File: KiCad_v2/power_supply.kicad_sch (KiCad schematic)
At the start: 45 parts, among them U1 TPS55340RTER, U6 MCP73871, U8 TPS54331

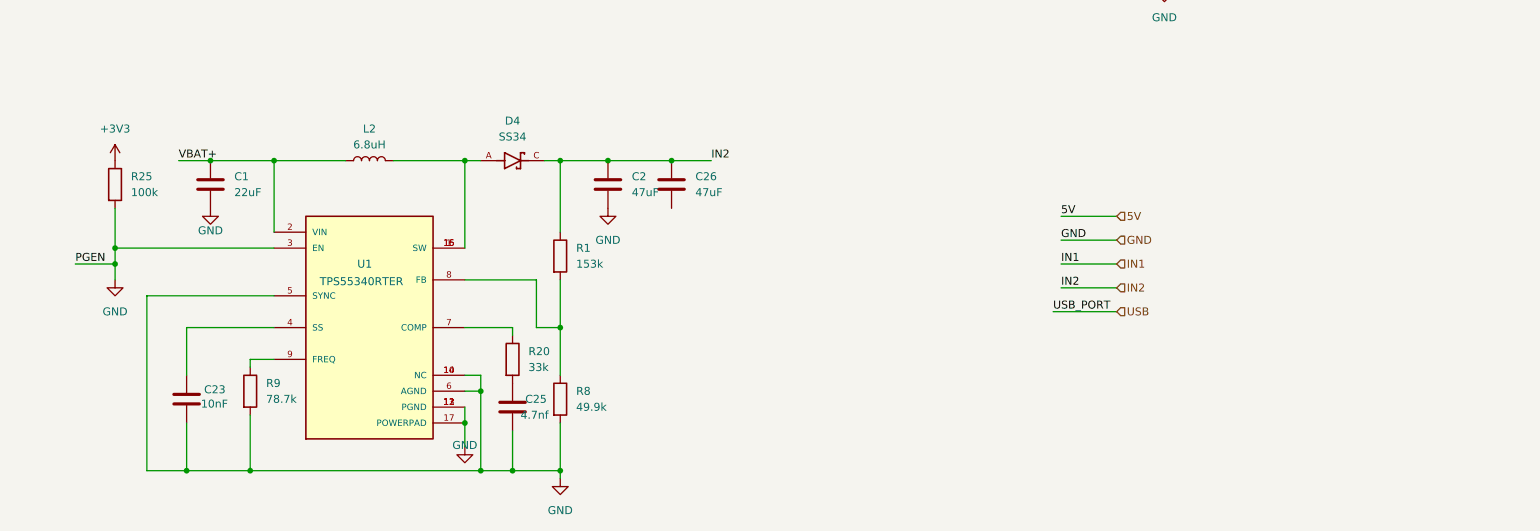
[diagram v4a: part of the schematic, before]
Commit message: agrego LT8582
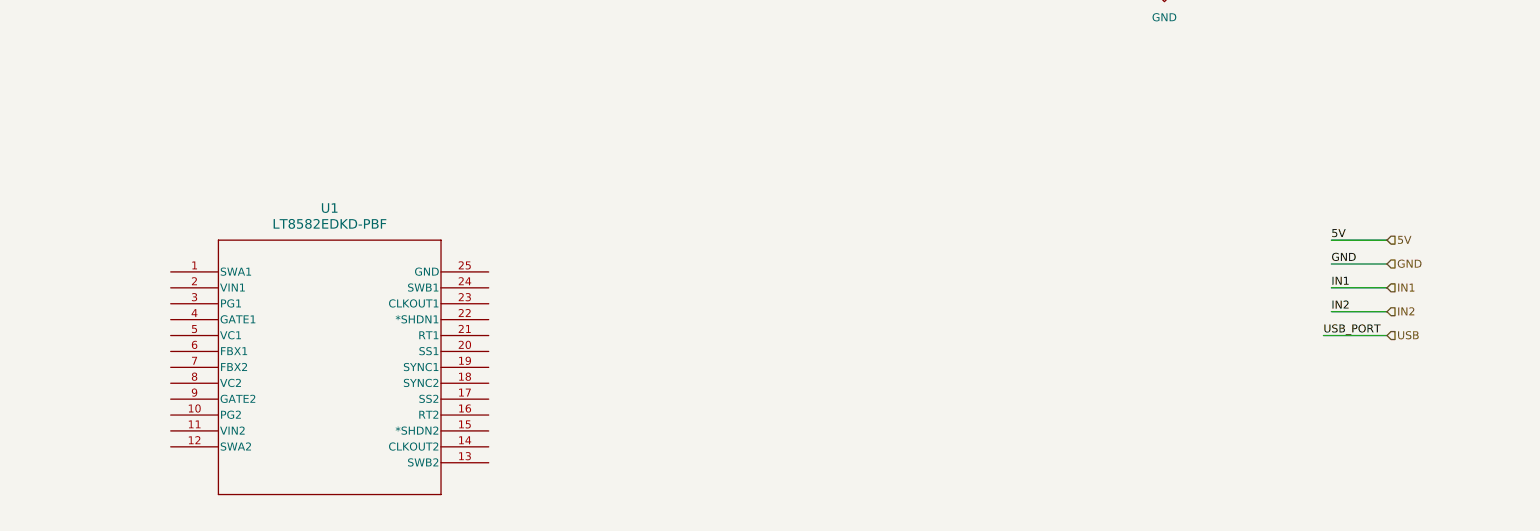
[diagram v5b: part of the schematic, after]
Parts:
- removed C1: 22uF, Capacitor_SMD:C_0603_1608Metric, symbol Device:C
- removed C2, C26: 47uF, Capacitor_SMD:C_0603_1608Metric, symbol Device:C
- removed C23: 10nF, Capacitor_SMD:C_0603_1608Metric, symbol Device:C
- removed C25: 4.7nf, Capacitor_SMD:C_0603_1608Metric, symbol Device:C
- removed D4: SS34, Custom_Footprints:DIOM7959X265N, symbol SS34:SS34
- removed L2: 6.8uH, Custom_Footprints:IND_SRP6540-100M, symbol Device:L
- removed R1: 153k, Resistor_SMD:R_0603_1608Metric, symbol Device:R
- removed R20: 33k, Resistor_SMD:R_0603_1608Metric, symbol Device:R
- removed R25: 100k, Resistor_SMD:R_0603_1608Metric, symbol Device:R
- removed R8: 49.9k, Resistor_SMD:R_0603_1608Metric, symbol Device:R
- removed R9: 78.7k, Resistor_SMD:R_0603_1608Metric, symbol Device:R
- removed U1: TPS55340RTER, Custom_Footprints:QFN50P300X300X80-17N, symbol TPS55340RTER:TPS55340RTER
- added U1: LT8582EDKD-PBF, Custom_Footprints:DKD_ADI-M, symbol LT8582:LT8582EDKD-PBF
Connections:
- net GND: no longer R6.1, U6.6 (~{PG})
- new net PGEN: R6.1, U6.6 (~{PG})

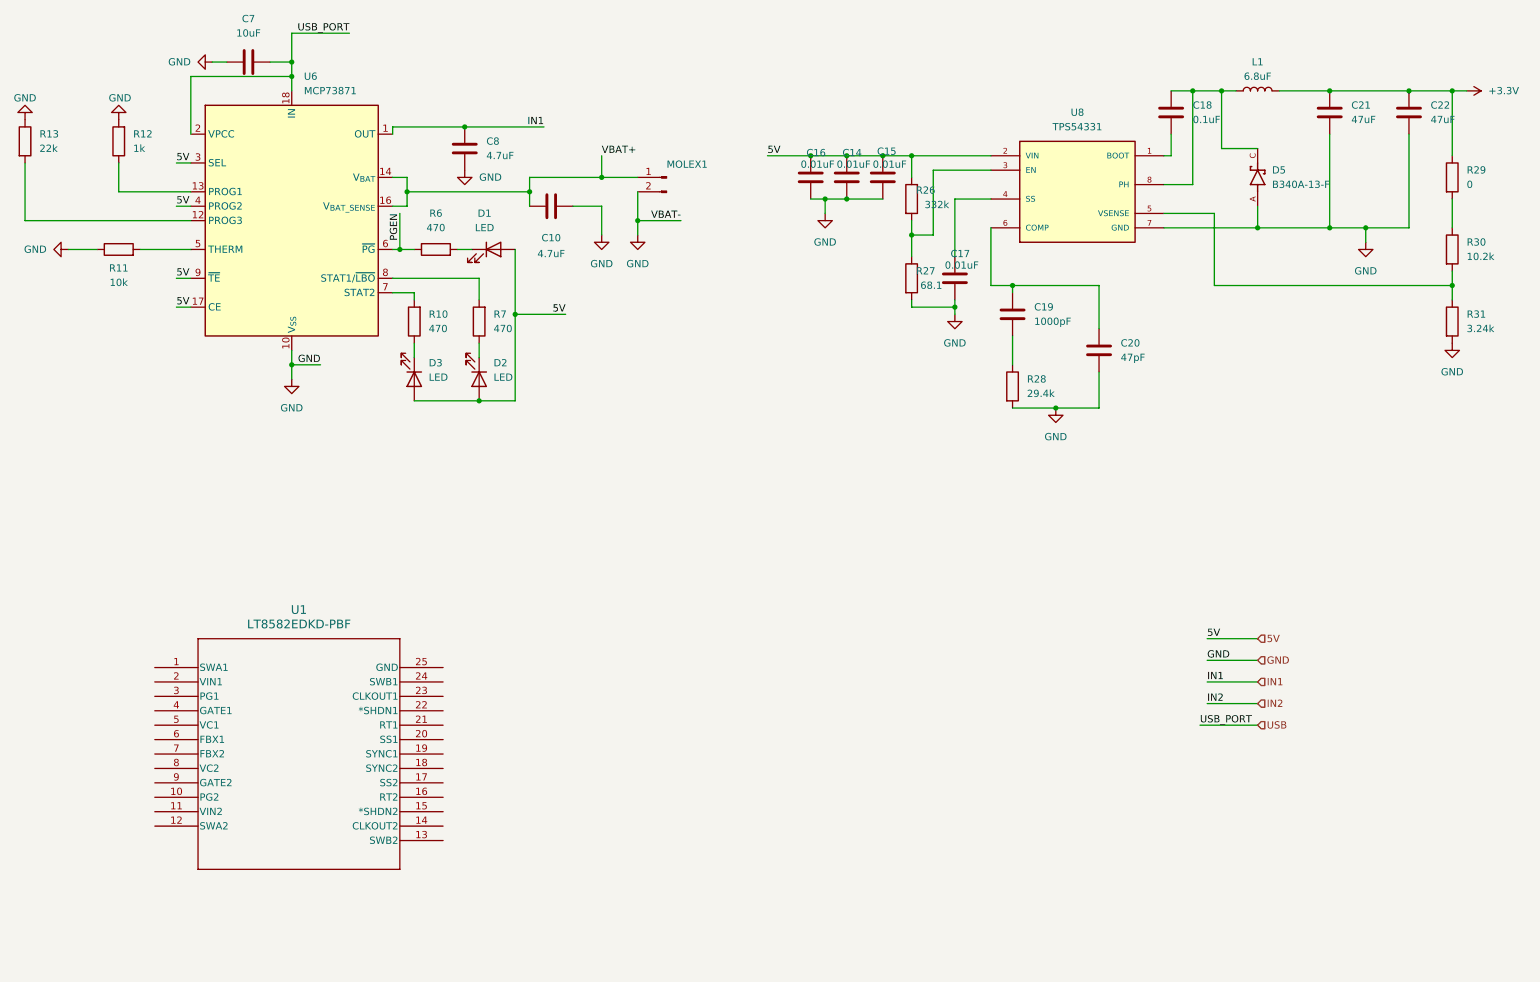
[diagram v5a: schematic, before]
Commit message: agrego .step y footprint de regulador 3v3
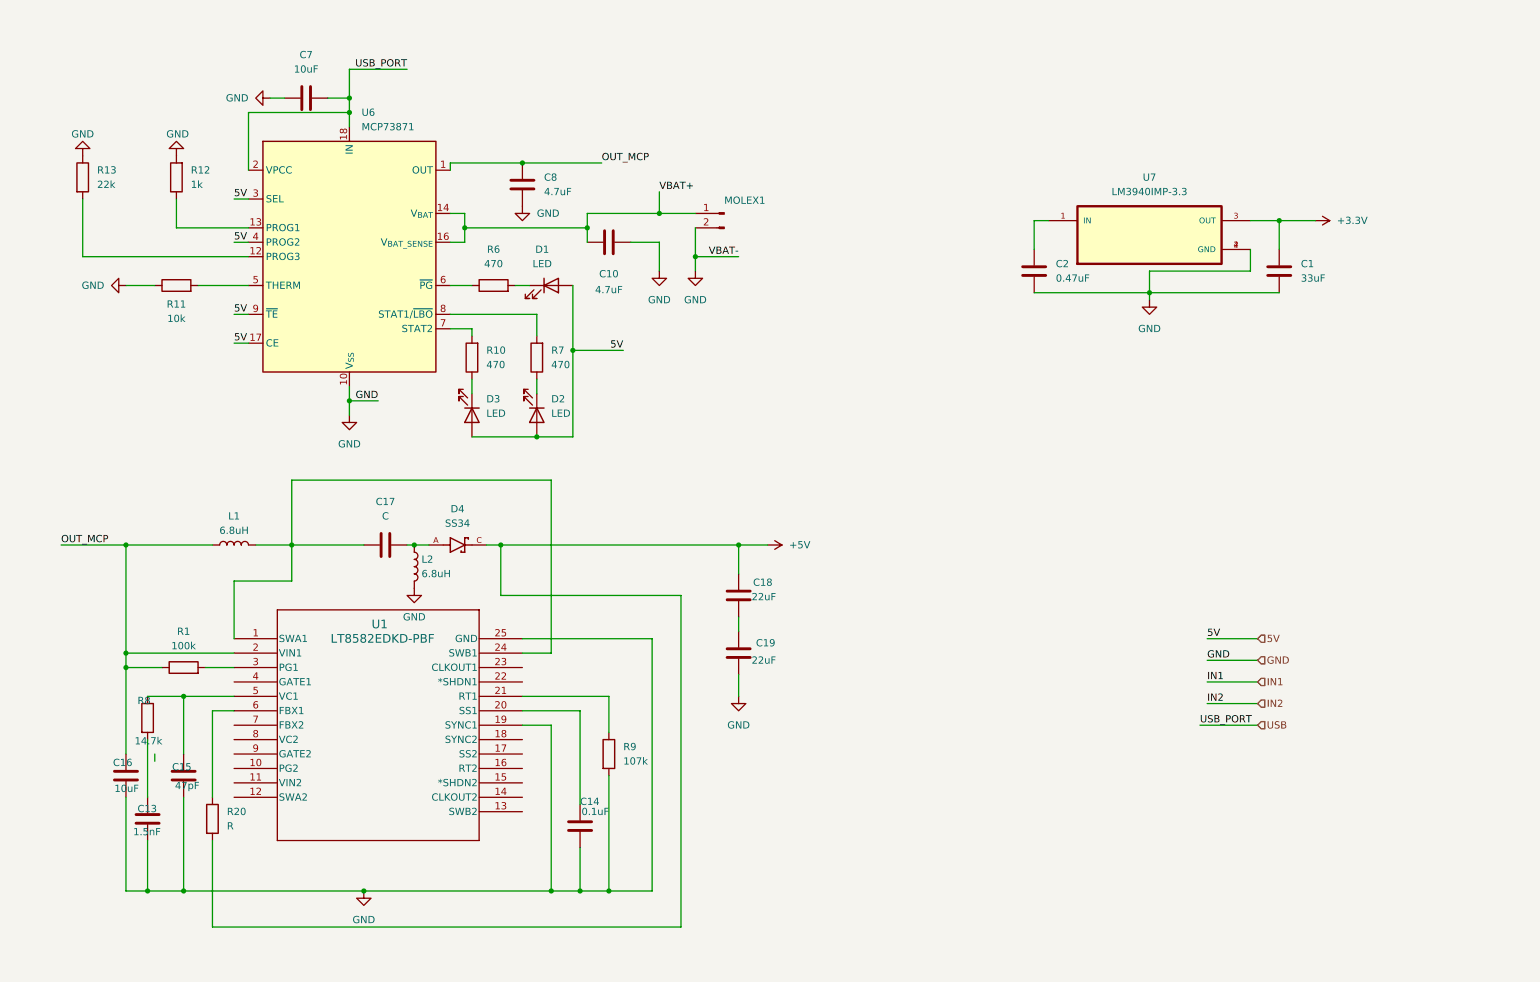
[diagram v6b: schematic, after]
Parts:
- removed C20: 47pF, Capacitor_SMD:C_0603_1608Metric, symbol Device:C
- removed C21, C22: 47uF, Capacitor_SMD:C_0603_1608Metric, symbol Device:C
- removed D5: B340A-13-F, Custom_Footprints:B340A, symbol B340A-13-F:B340A-13-F
- removed R26: 332k, Resistor_SMD:R_0603_1608Metric, symbol Device:R
- removed R27: 68.1, Resistor_SMD:R_0603_1608Metric, symbol Device:R
- removed R28: 29.4k, Resistor_SMD:R_0603_1608Metric, symbol Device:R
- removed R29: 0, Resistor_SMD:R_0603_1608Metric, symbol Device:R
- removed R30: 10.2k, Resistor_SMD:R_0603_1608Metric, symbol Device:R
- removed R31: 3.24k, Resistor_SMD:R_0603_1608Metric, symbol Device:R
- removed U8: TPS54331, Custom_Footprints:SOP8, symbol TPS54331:TPS54331
- added C1: 33uF, Capacitor_SMD:C_0603_1608Metric, symbol Device:C
- added C13: 1.5nF, Capacitor_SMD:C_0603_1608Metric, symbol Device:C
- added C2: 0.47uF, Capacitor_SMD:C_0603_1608Metric, symbol Device:C
- added D4: SS34, Custom_Footprints:SS34, symbol SS34:SS34
- added L2: 6.8uH, Custom_Footprints:IND_SRP6540-100M, symbol Device:L
- added R1: 100k, Resistor_SMD:R_0603_1608Metric, symbol Device:R
- added R20: R, Resistor_SMD:R_0603_1608Metric, symbol Device:R
- added R8: 14.7k, Resistor_SMD:R_0603_1608Metric, symbol Device:R
- added R9: 107k, Resistor_SMD:R_0603_1608Metric, symbol Device:R
- added U7: LM3940IMP-3.3, Custom_Footprints:SOT230P700X180-4N, symbol LM3940IMP-3.3:LM3940IMP-3.3
- C14: value 0.01uF -> 0.1uF
- C15: value 0.01uF -> 47pF
- C16: value 0.01uF -> 10uF
- C17: value 0.01uF -> C
- C18: value 0.1uF -> 22uF
- C19: value 1000pF -> 22uF
- L1: value 6.8uF -> 6.8uH
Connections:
- net +3.3V: now also C1.1, U7.3 (OUT); no longer L1.2
- net 5V: no longer C14.1, C15.1, C16.1
- net GND: now also C19.2, U1.19 (SYNC1), U1.25 (GND), C1.2, C13.2, C2.2, L2.2, R9.2, U7.2 (GND), U7.4 (GND); no longer C17.2
- net IN1: no longer C8.1, U6.1 (OUT), U6.20 (OUT)
- net at C17.1: now also L1.2, U1.1 (SWA1), U1.24 (SWB1)
- net +5V: now reaches C18.1
- net +5V: now also D4.C, R20.2; no longer L1.1
- net at C19.1: now also C18.2
- net OUT_MCP: now reaches U1.2 (VIN1)
- net OUT_MCP: now also C16.1, C8.1, L1.1, U6.1 (OUT), U6.20 (OUT), R1.1
- net at U1.20 (SS1): now also C14.1
- net at U1.21 (RT1): now also R9.1
- net at U1.3 (PG1): now also R1.2
- net at U1.5 (VC1): now also C15.1, R8.1
- net at U1.6 (FBX1): now also R20.1
- net PGEN: no longer names the net of R6.1, U6.6 (~{PG})
- new net: C17.2, D4.A, L2.1
- new net: C13.1, R8.2
- new net: C2.1, U7.1 (IN)
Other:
- moved on the sheet: C10, C7, C8, D1, D2, D3, MOLEX1, R10, R11, R12, R13, R6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

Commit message: circuito terminado de LT8582, falta calcular valores
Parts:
- C17: value C -> 2.2uF
- R20: value R -> 47.3k
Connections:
- net +5V: now also C2.1, U7.1 (IN)
- net OUT_MCP: now also R9.1, U1.21 (RT1), U1.22 (*SHDN1)
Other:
- moved on the sheet: C1, C17, C2, L2, U7

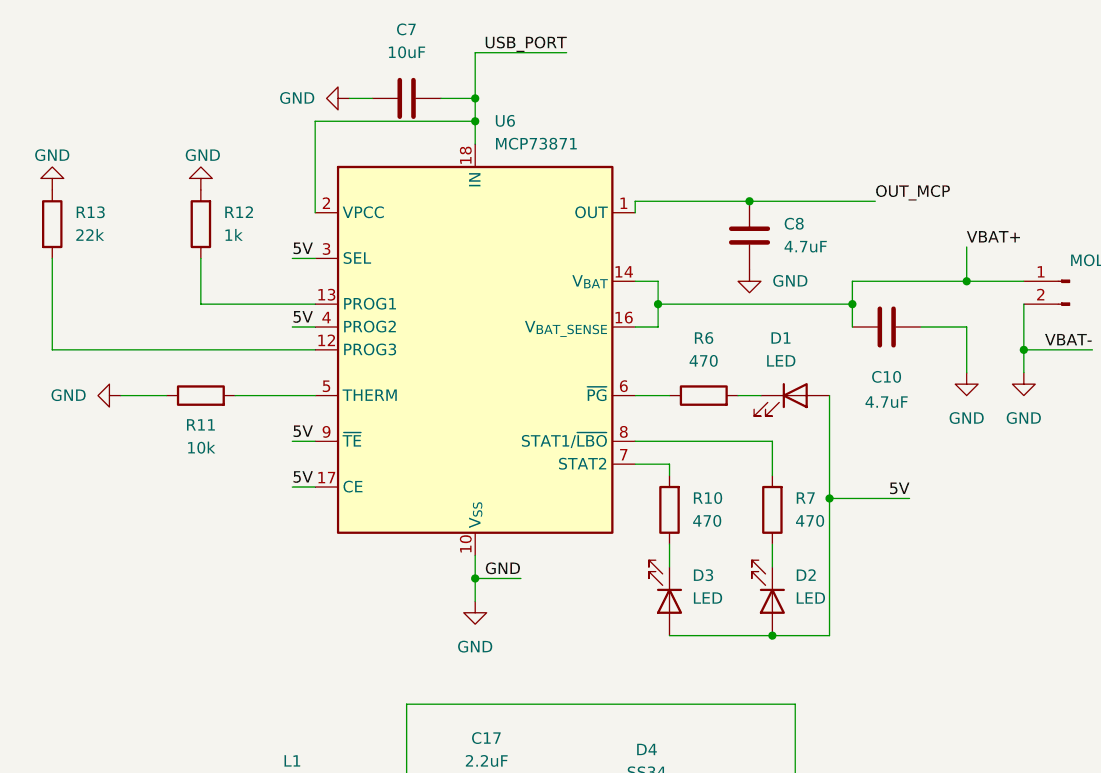
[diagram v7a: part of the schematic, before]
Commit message: feat: huella cm4 y mcp symbols
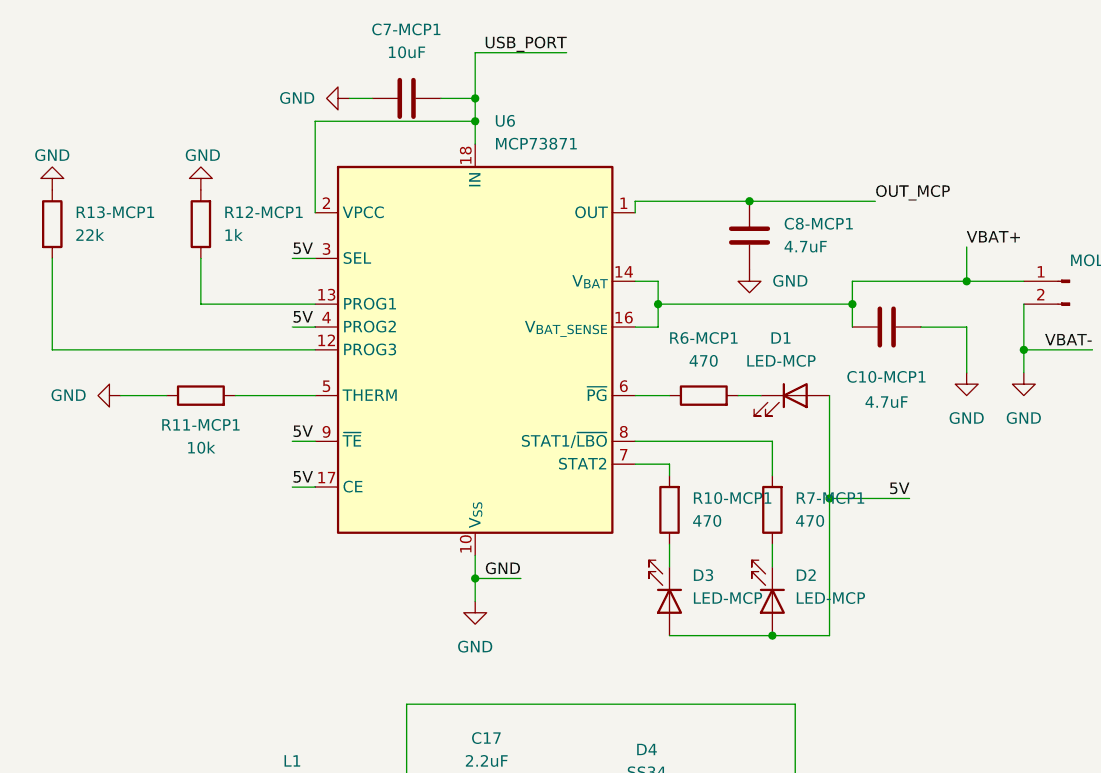
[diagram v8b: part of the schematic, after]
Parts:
- D1, D2, D3: value LED -> LED-MCP
- renumbered C10 to C10-MCP1, C7 to C7-MCP1, C8 to C8-MCP1, R10 to R10-MCP1, R11 to R11-MCP1, R12 to R12-MCP1, R13 to R13-MCP1, R6 to R6-MCP1, R7 to R7-MCP1
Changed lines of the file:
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@@
 			)
 		)
-		(property "Value" "LED"
+		(property "Value" "LED-MCP"
 			(at 113.03 86.0424 90)
 			(effects
@@
 			)
 		)
-		(property "Value" "LED"
+		(property "Value" "LED-MCP"
 			(at 111.4425 59.69 0)
 			(effects
@@
 		(dnp no)
 		(fields_autoplaced yes)
-		(property "Reference" "R10"
+		(property "Reference" "R10-MCP1"
 			(at 101.6 74.9299 0)
 			(effects
@@
 			(project "SignaLink"
 				(path "/a1f5fcc2-f8ff-418d-9afd-dd6d7b5c6dc3/950de23e-fb2c-4bf8-9e16-f2d0f97a3085"
-					(reference "R10")
+					(reference "R10-MCP1")
 					(unit 1)
 				)
@@
 		(dnp no)
 		(fields_autoplaced yes)
-		(property "Reference" "R12"
+		(property "Reference" "R12-MCP1"
 			(at 49.53 43.1799 0)
 			(effects
@@
 			(project ""
 				(path "/a1f5fcc2-f8ff-418d-9afd-dd6d7b5c6dc3/950de23e-fb2c-4bf8-9e16-f2d0f97a3085"
-					(reference "R12")
+					(reference "R12-MCP1")
 					(unit 1)
 				)
@@
 		(dnp no)
 		(fields_autoplaced yes)
-		(property "Reference" "R6"
+		(property "Reference" "R6-MCP1"
 			(at 102.87 57.15 90)
 			(effects
@@
 			(project ""
 				(path "/a1f5fcc2-f8ff-418d-9afd-dd6d7b5c6dc3/950de23e-fb2c-4bf8-9e16-f2d0f97a3085"
-					(reference "R6")
+					(reference "R6-MCP1")
 					(unit 1)
 				)
@@
 		(dnp no)
 		(fields_autoplaced yes)
-		(property "Reference" "C8"
+		(property "Reference" "C8-MCP1"
 			(at 111.76 44.4499 0)
 			(effects
@@
 			(project ""
 				(path "/a1f5fcc2-f8ff-418d-9afd-dd6d7b5c6dc3/950de23e-fb2c-4bf8-9e16-f2d0f97a3085"
-					(reference "C8")
+					(reference "C8-MCP1")
 					(unit 1)
 				)
@@
 		(on_board yes)
 		(dnp no)
-		(property "Reference" "C10"
+		(property "Reference" "C10-MCP1"
 			(at 123.19 61.468 90)
 			(effects
@@
 			(project ""
 				(path "/a1f5fcc2-f8ff-418d-9afd-dd6d7b5c6dc3/950de23e-fb2c-4bf8-9e16-f2d0f97a3085"
-					(reference "C10")
+					(reference "C10-MCP1")
 					(unit 1)
 				)
@@
 			)
 		)
-		(property "Value" "LED"
+		(property "Value" "LED-MCP"
 			(at 101.6 86.0424 90)
 			(effects
@@
 		(dnp no)
 		(fields_autoplaced yes)
-		(property "Reference" "R7"
+		(property "Reference" "R7-MCP1"
 			(at 113.03 74.9299 0)
 			(effects
@@
 			(project "SignaLink"
 				(path "/a1f5fcc2-f8ff-418d-9afd-dd6d7b5c6dc3/950de23e-fb2c-4bf8-9e16-f2d0f97a3085"
-					(reference "R7")
+					(reference "R7-MCP1")
 					(unit 1)
 				)
@@
 		(dnp no)
 		(fields_autoplaced yes)
-		(property "Reference" "C7"
+		(property "Reference" "C7-MCP1"
 			(at 69.85 22.86 90)
 			(effects
@@
 			(project ""
 				(path "/a1f5fcc2-f8ff-418d-9afd-dd6d7b5c6dc3/950de23e-fb2c-4bf8-9e16-f2d0f97a3085"
-					(reference "C7")
+					(reference "C7-MCP1")
 					(unit 1)
 				)
@@
 		(dnp no)
 		(fields_autoplaced yes)
-		(property "Reference" "R13"
+		(property "Reference" "R13-MCP1"
 			(at 33.02 43.1799 0)
 			(effects
@@
 			(project ""
 				(path "/a1f5fcc2-f8ff-418d-9afd-dd6d7b5c6dc3/950de23e-fb2c-4bf8-9e16-f2d0f97a3085"
-					(reference "R13")
+					(reference "R13-MCP1")
 					(unit 1)
 				)
@@
 		(on_board yes)
 		(dnp no)
-		(property "Reference" "R11"
+		(property "Reference" "R11-MCP1"
 			(at 46.99 66.802 90)
 			(effects
@@
 			(project ""
 				(path "/a1f5fcc2-f8ff-418d-9afd-dd6d7b5c6dc3/950de23e-fb2c-4bf8-9e16-f2d0f97a3085"
-					(reference "R11")
+					(reference "R11-MCP1")
 					(unit 1)
 				)
